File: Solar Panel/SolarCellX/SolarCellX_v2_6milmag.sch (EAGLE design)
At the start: 16 parts

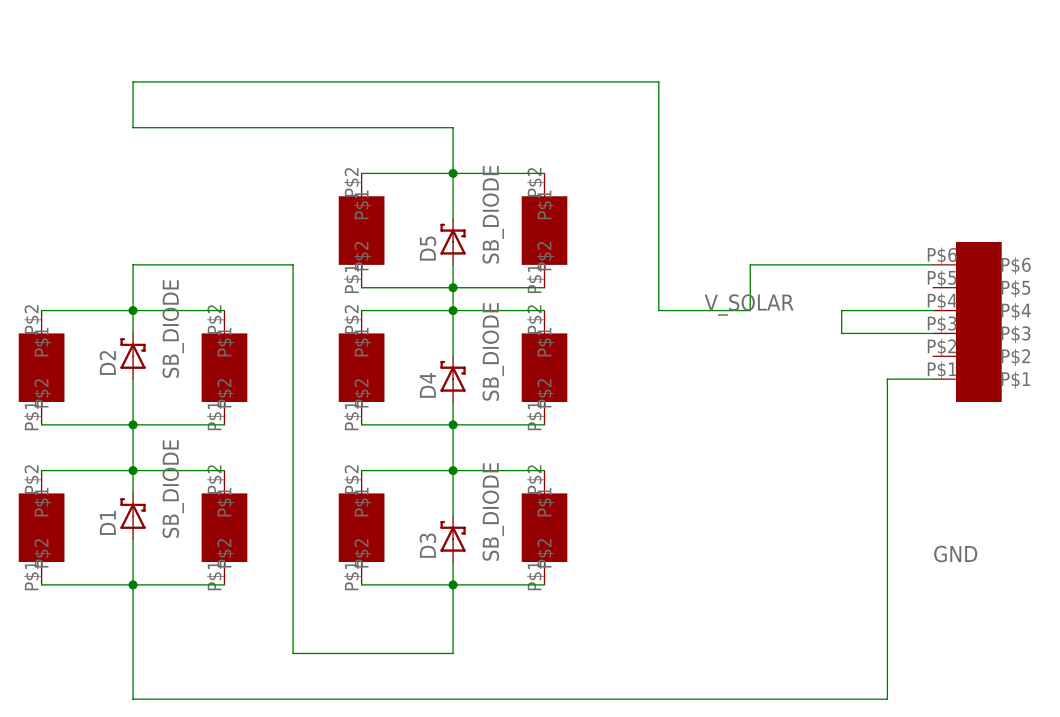
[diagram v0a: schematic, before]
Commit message: Changed pinout for X, added silkscreen
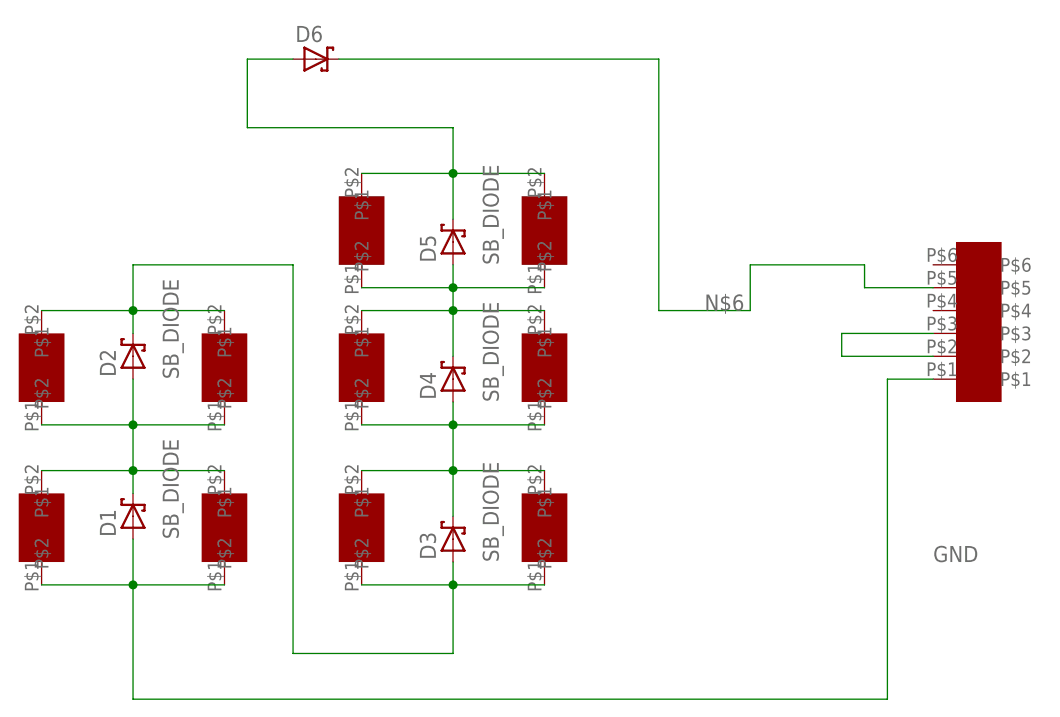
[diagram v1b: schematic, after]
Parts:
- added D6: SB_DIODE, Solar:SB_DIODE
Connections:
- new net N$6: D6.NEG, U$1.P$5
- net N$1: now also U$1.P$2; no longer U$1.P$4
- net V_SOLAR: now also D6.POS; no longer U$1.P$6
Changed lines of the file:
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@@
 <?xml version="1.0" encoding="utf-8"?>
 <!DOCTYPE eagle SYSTEM "eagle.dtd">
-<eagle version="9.3.1">
+<eagle version="9.2.2">
 <drawing>
 <settings>
@@
 <part name="2" library="Solar" deviceset="SLMD121H04L" device=""/>
 <part name="U$1" library="Solar" deviceset="M20-8760342" device=""/>
+<part name="D6" library="Solar" deviceset="SB_DIODE" device=""/>
 </parts>
 <sheets>
@@
 <instance part="2" gate="G$1" x="73.66" y="58.42" smashed="yes" rot="R90"/>
 <instance part="U$1" gate="G$1" x="116.84" y="43.18" smashed="yes"/>
+<instance part="D6" gate="G$1" x="45.72" y="81.28" smashed="yes">
+<attribute name="NAME" x="43.434" y="83.185" size="1.778" layer="95"/>
+</instance>
 </instances>
 <busses>
@@
 <net name="V_SOLAR" class="0">
 <segment>
-<wire x1="25.4" y1="78.74" x2="83.82" y2="78.74" width="0.1524" layer="91"/>
-<wire x1="83.82" y1="78.74" x2="83.82" y2="53.34" width="0.1524" layer="91"/>
-<label x="88.9" y="53.34" size="1.778" layer="95"/>
 <pinref part="1" gate="G$1" pin="P$2"/>
 <pinref part="2" gate="G$1" pin="P$2"/>
@@
 <wire x1="60.96" y1="63.5" x2="60.96" y2="68.58" width="0.1524" layer="91"/>
 <junction x="60.96" y="68.58"/>
-<wire x1="60.96" y1="68.58" x2="60.96" y2="73.66" width="0.1524" layer="91"/>
-<wire x1="60.96" y1="73.66" x2="25.4" y2="73.66" width="0.1524" layer="91"/>
-<wire x1="25.4" y1="73.66" x2="25.4" y2="78.74" width="0.1524" layer="91"/>
-<wire x1="83.82" y1="53.34" x2="93.98" y2="53.34" width="0.1524" layer="91"/>
-<wire x1="93.98" y1="53.34" x2="93.98" y2="58.42" width="0.1524" layer="91"/>
-<pinref part="U$1" gate="G$1" pin="P$6"/>
-<wire x1="93.98" y1="58.42" x2="114.3" y2="58.42" width="0.1524" layer="91"/>
+<pinref part="D6" gate="G$1" pin="POS"/>
+<wire x1="43.18" y1="81.28" x2="38.1" y2="81.28" width="0.1524" layer="91"/>
+<wire x1="38.1" y1="81.28" x2="38.1" y2="73.66" width="0.1524" layer="91"/>
+<wire x1="38.1" y1="73.66" x2="60.96" y2="73.66" width="0.1524" layer="91"/>
+<wire x1="60.96" y1="73.66" x2="60.96" y2="68.58" width="0.1524" layer="91"/>
 </segment>
 </net>
 <net name="N$1" class="0">
 <segment>
-<pinref part="U$1" gate="G$1" pin="P$4"/>
-<wire x1="114.3" y1="53.34" x2="104.14" y2="53.34" width="0.1524" layer="91"/>
-<wire x1="104.14" y1="53.34" x2="104.14" y2="50.8" width="0.1524" layer="91"/>
 <pinref part="U$1" gate="G$1" pin="P$3"/>
 <wire x1="104.14" y1="50.8" x2="114.3" y2="50.8" width="0.1524" layer="91"/>
-</segment>
-</net>
+<pinref part="U$1" gate="G$1" pin="P$2"/>
+<wire x1="104.14" y1="50.8" x2="104.14" y2="48.26" width="0.1524" layer="91"/>
+<wire x1="104.14" y1="48.26" x2="114.3" y2="48.26" width="0.1524" layer="91"/>
+</segment>
+</net>
+<net name="N$6" class="0">
+<segment>
+<wire x1="93.98" y1="53.34" x2="93.98" y2="58.42" width="0.1524" layer="91"/>
+<wire x1="83.82" y1="81.28" x2="83.82" y2="53.34" width="0.1524" layer="91"/>
+<wire x1="83.82" y1="53.34" x2="93.98" y2="53.34" width="0.1524" layer="91"/>
+<label x="88.9" y="53.34" size="1.778" layer="95"/>
+<pinref part="D6" gate="G$1" pin="NEG"/>
+<wire x1="48.26" y1="81.28" x2="83.82" y2="81.28" width="0.1524" layer="91"/>
+<wire x1="93.98" y1="58.42" x2="106.68" y2="58.42" width="0.1524" layer="91"/>
+<wire x1="106.68" y1="58.42" x2="106.68" y2="55.88" width="0.1524" layer="91"/>
+<pinref part="U$1" gate="G$1" pin="P$5"/>
+<wire x1="106.68" y1="55.88" x2="114.3" y2="55.88" width="0.1524" layer="91"/>
+</segment>
+</net>
